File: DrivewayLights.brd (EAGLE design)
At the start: 69.8 x 83.8 mm, 29 parts, among them U1 TLC59108PW

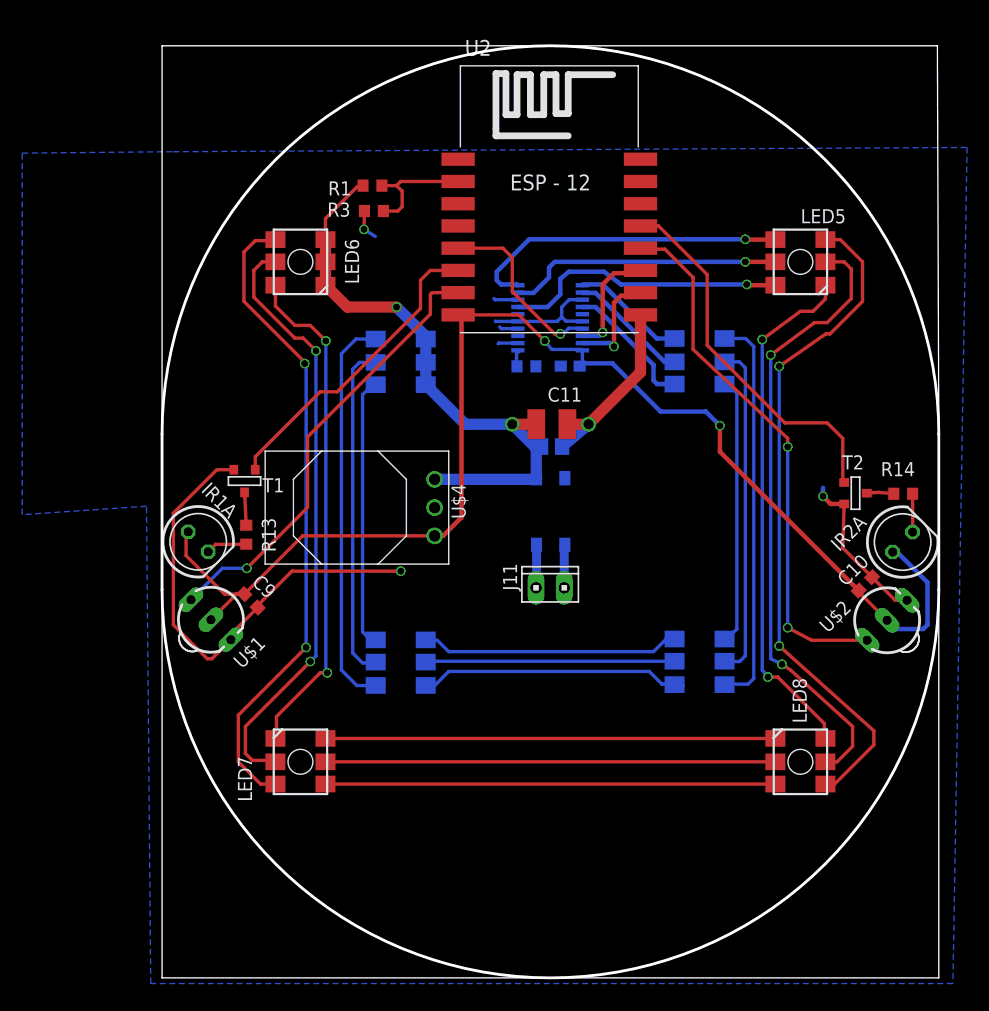
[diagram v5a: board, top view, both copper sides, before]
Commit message: Updates to schematic and board layout - a lot of signals ripped up for using correct footprint and adding buttons and interface for programming.
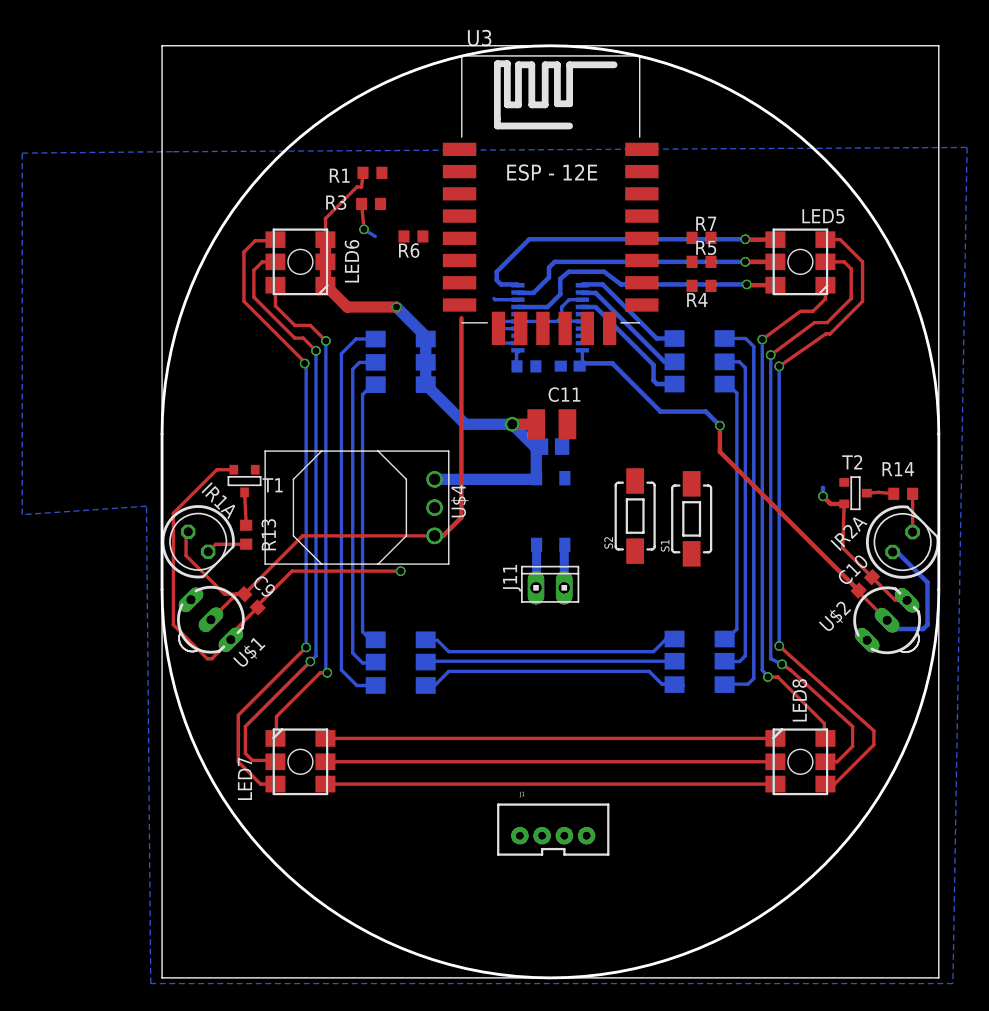
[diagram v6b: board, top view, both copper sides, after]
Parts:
- removed U2: (no value), esp8266modules:ESP12-SMD
- added J1: (no value), SparkFun-Connectors:JST-4-PTH-VERT
- added R4, R5, R6, R7: 1k, resistor:R0603
- added S1, S2: SWITCH-MOMENTARY-2SMD-1101NE, SparkFun-Electromechanical:TACTILE-SWITCH-1101NE
- added U3: (no value), esp8266modules:ESP12E-SMD
- moved R1 1.14 mm to (18.9, 72.4)
- moved R3 0.68 mm to (18.8, 69.6)
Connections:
- removed net N$7: R1.1, R3.2, U2.ADC
- new net ADC: R1.1, R3.2, U3.ADC
- new net FLASH_N: R7.1, U3.GPIO0
- new net IRLED0: R4.2, U3.GPIO15
- new net RESET_N: U3.RESET
- new net RX: J1.2, U3.RXD0
- new net TX: J1.3, U3.TXD0
- net 3.3V: now also J1.4, R5.2, R6.2, R7.2, U3.CH_PD, U3.VCC; no longer U2.VCC
- net GND: now also J1.1, R4.1, U3.GND; no longer U2.GND
- net IRLED1: now also U3.GPIO12; no longer U2.GPIO12
- net IRLED2: now also U3.GPIO13; no longer U2.GPIO5
- net IR_IN1: now also U3.GPIO4; no longer U2.GPIO13
- net IR_IN2: now also U3.GPIO5; no longer U2.GPIO0
- net LED_NRESET: no longer U2.GPIO14
- net LED_SCL: now also R6.1, U3.GPIO14; no longer U2.GPIO2
- net LED_SDA: now also R5.1, U3.GPIO2; no longer U2.GPIO15
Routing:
- net IR_IN2: track 48.7 -> 0.00 mm, vias 2 -> 0
- net IR_IN1: track 40.2 -> 0.00 mm, vias 1 -> 0
- net IRLED2: track 33.8 -> 0.00 mm
- net IRLED1: track 27.8 -> 0.00 mm
- net LED_NRESET: track 16.4 -> 0.00 mm, vias 1 -> 0
- net GND: track 93.6 -> 77.5 mm, vias 4 -> 3
- net 3.3V: track 118.2 -> 105.3 mm, vias 2 -> 1
- net N$7: track 11.0 -> 0.00 mm
- net LED_SCL: track 10.2 -> 0.00 mm, vias 1 -> 0
- net LED_SDA: track 9.67 -> 0.00 mm, vias 1 -> 0
- net VCAP: track 52.7 -> 53.8 mm
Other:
- outline, holes or cut-outs redrawn

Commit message: Changed LED routing a bit to help route other traces.
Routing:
- net N$29: track 40.5 -> 47.4 mm, vias 0 -> 2
- net N$26: track 40.5 -> 46.8 mm, vias 0 -> 2
- net N$32: track 40.5 -> 45.5 mm, vias 0 -> 2
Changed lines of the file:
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@@
 </class>
 </classes>
-<designrules name="SeeedStudio_2layer_DRU_no_angle_20140221">
+<designrules name="SeeedStudio_2layer_DRU_no_angle_20140221 *">
 <description language="de">&lt;b&gt;EAGLE Design Rules&lt;/b&gt;
 &lt;p&gt;
@@
 <param name="mdDrill" value="10mil"/>
 <param name="mdSmdStop" value="0mil"/>
-<param name="msWidth" value="6mil"/>
+<param name="msWidth" value="12mil"/>
 <param name="msDrill" value="12mil"/>
 <param name="msMicroVia" value="12mil"/>
@@
 <wire x1="31.9996" y1="57.0848" x2="31.9996" y2="57.7348" width="0" layer="19" extent="16-16"/>
 <wire x1="29.9472" y1="60.9848" x2="29.972" y2="59.055" width="0" layer="19" extent="16-16"/>
-<wire x1="33.616" y1="54.991" x2="31.9996" y2="57.0848" width="0" layer="19" extent="16-16"/>
-<wire x1="35.853" y1="55.0164" x2="33.616" y2="54.991" width="0" layer="19" extent="16-16"/>
-<wire x1="36.452" y1="49.784" x2="35.853" y2="55.0164" width="0" layer="19" extent="1-16"/>
-<wire x1="35.9766" y1="47.7774" x2="36.452" y2="49.784" width="0" layer="19" extent="1-16"/>
-<wire x1="36.2204" y1="44.9354" x2="35.9766" y2="47.7774" width="0" layer="19" extent="16-16"/>
-<wire x1="24.511" y1="42.291" x2="36.2204" y2="44.9354" width="0" layer="19" extent="16-16"/>
-<wire x1="21.463" y1="36.576" x2="24.511" y2="42.291" width="0" layer="19" extent="1-1"/>
-<wire x1="19.177" y1="66.675" x2="29.845" y2="61.087" width="0" layer="19" extent="16-16"/>
-<wire x1="59.436" y1="44.069" x2="49.364" y2="62.23" width="0" layer="19" extent="1-16"/>
-<wire x1="32.179" y1="12.785" x2="4.064" y2="28.702" width="0" layer="19" extent="1-1"/>
+<wire x1="36.452" y1="49.784" x2="35.9766" y2="47.7774" width="0" layer="19" extent="1-16"/>
 </signal>
 <signal name="3.3V">
@@
 <wire x1="21.756" y1="66.675" x2="26.752" y2="60.507" width="0" layer="19" extent="1-1"/>
 <wire x1="26.752" y1="70.507" x2="21.756" y2="66.675" width="0" layer="19" extent="1-1"/>
-<wire x1="38.179" y1="12.785" x2="4.3942" y2="32.2072" width="0" layer="19" extent="1-1"/>
+<wire x1="38.179" y1="12.785" x2="25.273" y2="39.751" width="0" layer="19" extent="1-1"/>
 </signal>
 <signal name="LED_CURRENT_R">
@@
 <contactref element="LED8" pad="3"/>
 <contactref element="LED7" pad="4"/>
-<wire x1="14.696" y1="17.431" x2="55.154" y2="17.431" width="0.3048" layer="1"/>
+<wire x1="14.696" y1="17.431" x2="15.653" y2="17.431" width="0.3048" layer="1"/>
+<wire x1="15.653" y1="17.431" x2="20.193" y2="21.971" width="0.3048" layer="1"/>
+<wire x1="20.193" y1="21.971" x2="26.289" y2="21.971" width="0.3048" layer="1"/>
+<wire x1="26.289" y1="21.971" x2="26.543" y2="22.225" width="0.3048" layer="1"/>
+<via x="26.543" y="22.225" extent="1-16" drill="0.6"/>
+<wire x1="26.543" y1="22.225" x2="29.21" y2="24.892" width="0.3048" layer="16"/>
+<wire x1="29.21" y1="24.892" x2="41.402" y2="24.892" width="0.3048" layer="16"/>
+<wire x1="41.402" y1="24.892" x2="42.164" y2="24.13" width="0.3048" layer="16"/>
+<wire x1="42.164" y1="24.13" x2="42.164" y2="23.876" width="0.3048" layer="16"/>
+<via x="42.164" y="23.876" extent="1-16" drill="0.6"/>
+<wire x1="42.164" y1="23.876" x2="48.609" y2="17.431" width="0.3048" layer="1"/>
+<wire x1="48.609" y1="17.431" x2="55.154" y2="17.431" width="0.3048" layer="1"/>
 </signal>
 <signal name="N$27">
@@
 <contactref element="LED7" pad="5"/>
 <contactref element="LED8" pad="2"/>
-<wire x1="55.154" y1="19.431" x2="14.696" y2="19.431" width="0.3048" layer="1"/>
+<wire x1="14.696" y1="19.431" x2="15.494" y2="19.431" width="0.3048" layer="1"/>
+<wire x1="15.494" y1="19.431" x2="18.923" y2="22.86" width="0.3048" layer="1"/>
+<wire x1="18.923" y1="22.86" x2="25.019" y2="22.86" width="0.3048" layer="1"/>
+<wire x1="25.019" y1="22.86" x2="25.273" y2="23.114" width="0.3048" layer="1"/>
+<via x="25.273" y="23.114" extent="1-16" drill="0.6"/>
+<wire x1="25.273" y1="23.114" x2="25.273" y2="23.368" width="0.3048" layer="16"/>
+<wire x1="25.273" y1="23.368" x2="27.051" y2="25.908" width="0.3048" layer="16"/>
+<wire x1="27.051" y1="25.908" x2="42.799" y2="25.781" width="0.3048" layer="16"/>
+<wire x1="42.799" y1="25.781" x2="43.307" y2="24.638" width="0.3048" layer="16"/>
+<wire x1="43.307" y1="24.638" x2="43.434" y2="23.622" width="0.3048" layer="16"/>
+<wire x1="43.434" y1="23.622" x2="43.434" y2="24.003" width="0.3048" layer="16"/>
+<via x="43.434" y="24.003" extent="1-16" drill="0.6"/>
+<wire x1="43.434" y1="24.003" x2="48.006" y2="19.558" width="0.3048" layer="1"/>
+<wire x1="48.006" y1="19.558" x2="55.154" y2="19.431" width="0.3048" layer="1"/>
 </signal>
 <signal name="N$30">
@@
 <contactref element="LED8" pad="1"/>
 <contactref element="LED7" pad="6"/>
-<wire x1="14.696" y1="21.531" x2="55.154" y2="21.531" width="0.3048" layer="1"/>
+<wire x1="55.154" y1="21.531" x2="47.176" y2="21.531" width="0.3048" layer="1"/>
+<wire x1="47.176" y1="21.531" x2="45.085" y2="24.003" width="0.3048" layer="1"/>
+<via x="45.085" y="24.003" extent="1-16" drill="0.6"/>
+<wire x1="45.085" y1="24.003" x2="44.45" y2="24.638" width="0.3048" layer="16"/>
+<wire x1="44.45" y1="24.638" x2="43.18" y2="26.67" width="0.3048" layer="16"/>
+<wire x1="43.18" y1="26.67" x2="26.543" y2="26.67" width="0.3048" layer="16"/>
+<wire x1="26.543" y1="26.67" x2="26.035" y2="25.781" width="0.3048" layer="16"/>
+<wire x1="26.035" y1="25.781" x2="26.162" y2="25.908" width="0.3048" layer="16"/>
+<wire x1="26.035" y1="25.781" x2="24.257" y2="24.003" width="0.3048" layer="16"/>
+<via x="24.257" y="24.003" extent="1-16" drill="0.6"/>
+<wire x1="24.257" y1="24.003" x2="18.542" y2="23.876" width="0.3048" layer="1"/>
+<wire x1="18.542" y1="23.876" x2="16.129" y2="21.463" width="0.3048" layer="1"/>
+<wire x1="16.129" y1="21.463" x2="14.764" y2="21.463" width="0.3048" layer="1"/>
+<wire x1="14.764" y1="21.463" x2="14.696" y2="21.531" width="0.3048" layer="1"/>
 </signal>
 <signal name="N$33">
